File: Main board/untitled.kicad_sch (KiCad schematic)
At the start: 54 parts, among them J1 Conn_02x20_Odd_Even, J10 RA, J11 EL, J12 AZ, J13 GPS, J14 SHUTTER, J15 PWR_ON, J16 BOOT, J2 RJE05-166-1310, J9 DEC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

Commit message: updt
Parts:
- added C53: 100n, Capacitor_SMD:C_0402_1005Metric, symbol Device:C
- added R59, R60: 100k, Resistor_SMD:R_0402_1005Metric, symbol Device:R
- R43, R44: value 2k -> 2k2
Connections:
- net +3V3: now also R34.1, R35.1, R36.1, R37.1
- net DC_LED: now also U1.56 (PB4); no longer U1.57 (PB5)
- net GND: now also C53.2, R60.2; no longer R34.1, R35.1, R36.1, R37.1
- net USB_LED: now also U1.57 (PB5); no longer U1.56 (PB4)
- net VIN_ADC: now reaches U1.11 (PC3)
- net VIN_ADC: now also C53.1, R59.2, R60.1
- new net +12V: R59.1
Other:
- moved on the sheet: J10, J11, J12, J9, R34, R35, R36, R37

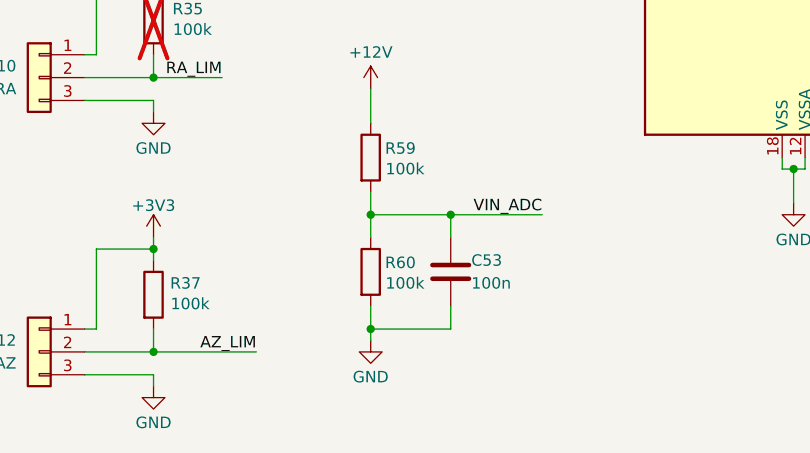
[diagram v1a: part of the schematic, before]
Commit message: Updated resistor values
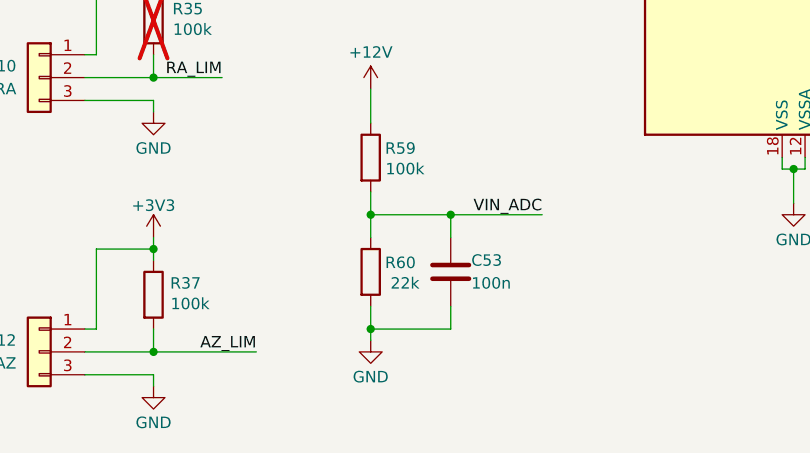
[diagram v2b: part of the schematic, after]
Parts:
- R60: value 100k -> 22k
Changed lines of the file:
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@@
 			)
 		)
-		(property "Value" "100k"
+		(property "Value" "22k"
 			(at 106.68 167.64 0)
 			(effects

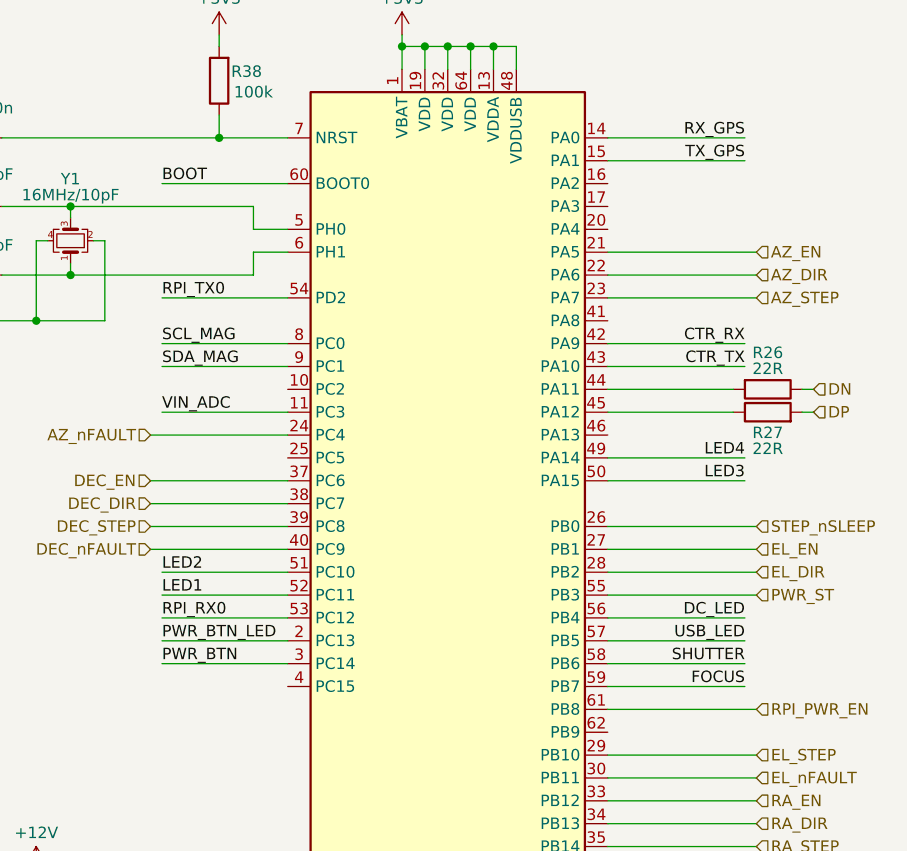
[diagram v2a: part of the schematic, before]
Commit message: Updated endstops routing
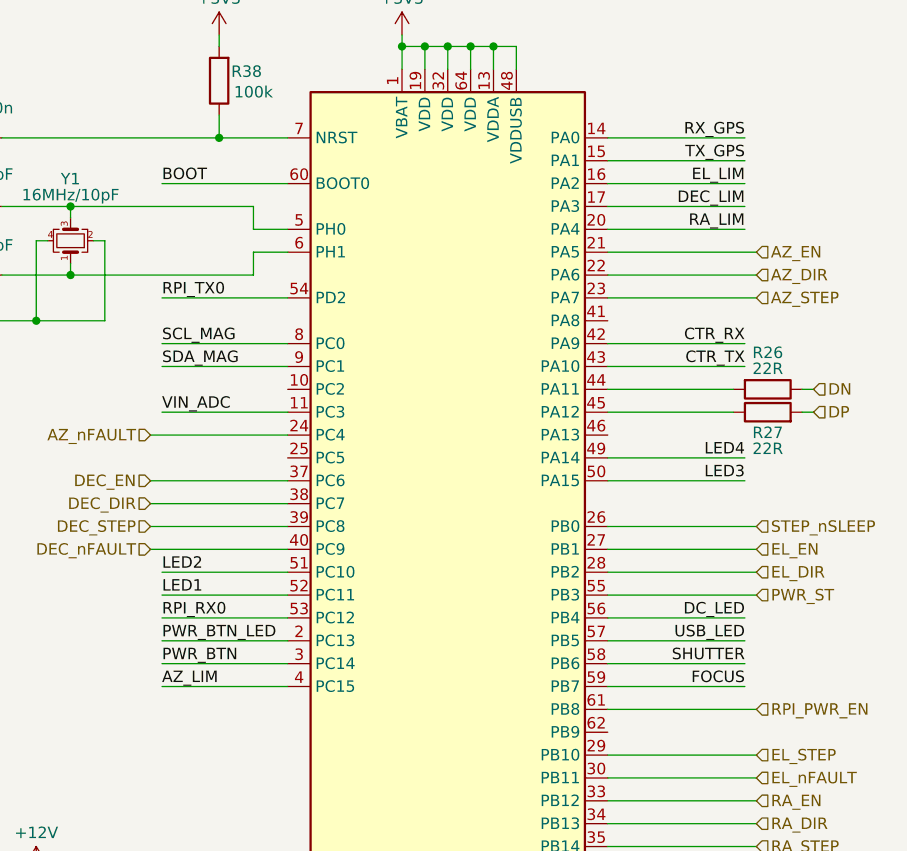
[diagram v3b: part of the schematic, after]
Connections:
- net AZ_LIM: now also U1.4 (PC15)
- net DEC_LIM: now also U1.17 (PA3)
- net EL_LIM: now also U1.16 (PA2)
- net RA_LIM: now also U1.20 (PA4)
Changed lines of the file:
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@@
+	(wire
+		(pts
+			(xy 166.37 74.93) (xy 181.61 74.93)
+		)
+		(stroke
+			(width 0)
+			(type default)
+		)
+	)
 	(wire
 		(pts
@@
 	(wire
 		(pts
+			(xy 166.37 69.85) (xy 181.61 69.85)
+		)
+		(stroke
+			(width 0)
+			(type default)
+		)
+	)
+	(wire
+		(pts
 			(xy 254 135.89) (xy 254 137.16)
 		)
@@
 	(wire
 		(pts
+			(xy 166.37 72.39) (xy 181.61 72.39)
+		)
+		(stroke
+			(width 0)
+			(type default)
+		)
+	)
+	(wire
+		(pts
 			(xy 43.18 163.83) (xy 43.18 165.1)
 		)
@@
 		(pts
 			(xy 127 72.39) (xy 127 74.93)
+		)
+		(stroke
+			(width 0)
+			(type default)
+		)
+	)
+	(wire
+		(pts
+			(xy 116.84 125.73) (xy 130.81 125.73)
 		)
 		(stroke
@@
 		)
 	)
+	(label "DEC_LIM"
+		(at 181.61 72.39 180)
+		(effects
+			(font
+				(size 1.27 1.27)
+			)
+			(justify right bottom)
+		)
+	)
 	(label "CAM_GND"
 		(at 33.02 106.68 0)
@@
 		)
 	)
+	(label "EL_LIM"
+		(at 181.61 69.85 180)
+		(effects
+			(font
+				(size 1.27 1.27)
+			)
+			(justify right bottom)
+		)
+	)
 	(label "PWR_BTN"
 		(at 116.84 123.19 0)
@@
 		)
 	)
+	(label "RA_LIM"
+		(at 181.61 74.93 180)
+		(effects
+			(font
+				(size 1.27 1.27)
+			)
+			(justify right bottom)
+		)
+	)
 	(label "LED3"
 		(at 200.66 101.6 0)
@@
 		(effects
 			(font
+				(size 1.27 1.27)
+			)
+			(justify left bottom)
+		)
+	)
+	(label "AZ_LIM"
+		(at 116.84 125.73 0)
+		(effects
+			(font

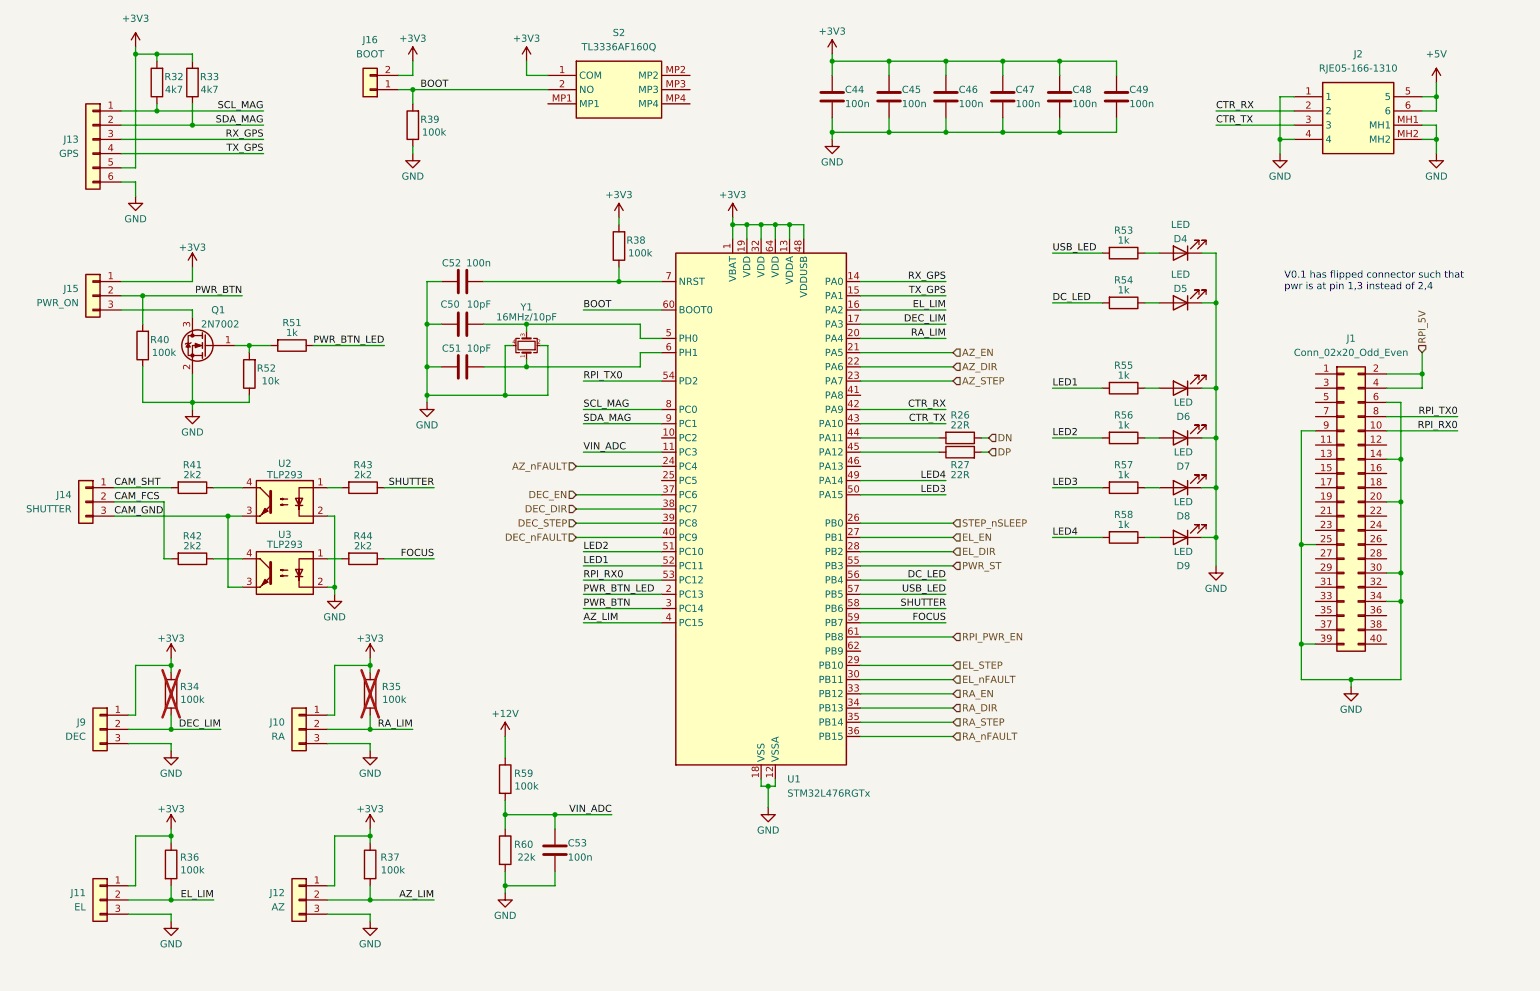
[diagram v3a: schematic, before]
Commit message: Main board updated to v0.3
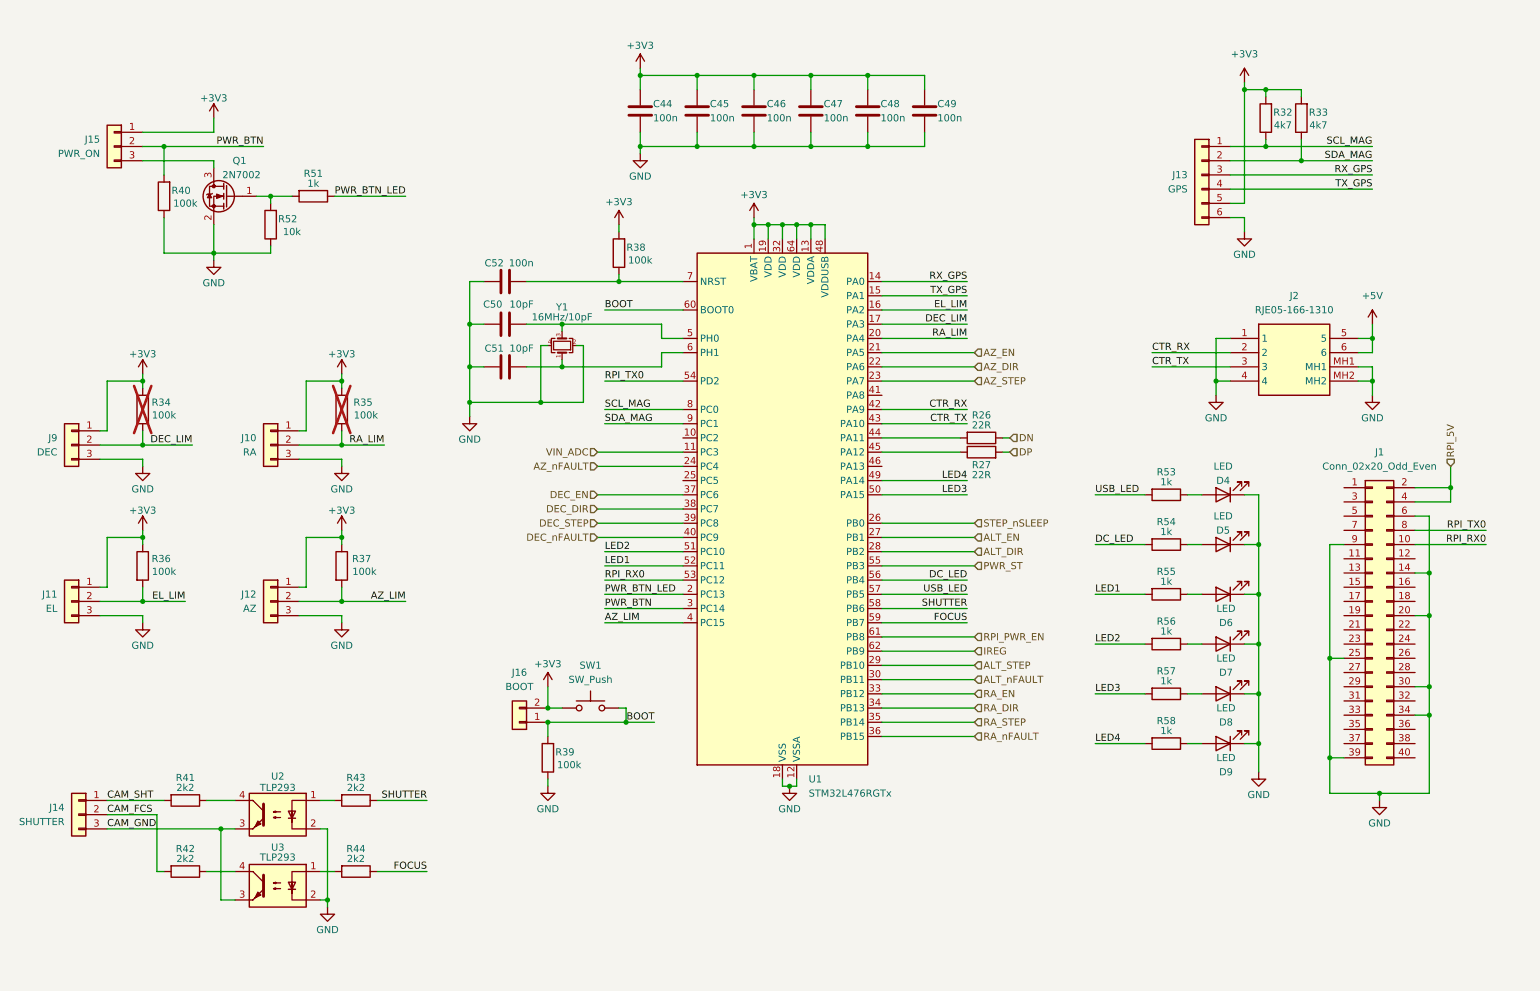
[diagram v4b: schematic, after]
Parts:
- removed C53: 100n, Capacitor_SMD:C_0402_1005Metric, symbol Device:C
- removed R59: 100k, Resistor_SMD:R_0402_1005Metric, symbol Device:R
- removed R60: 22k, Resistor_SMD:R_0402_1005Metric, symbol Device:R
- removed S2: TL3336AF160Q, TL3336AF160Q, symbol SamacSys_Parts:TL3336AF160Q
- added SW1: SW_Push, TL3336AF160Q, symbol Switch:SW_Push
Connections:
- net +3V3: now also SW1.1
- net BOOT: now also SW1.2
- net IREG: now reaches U1.62 (PB9)
- net EL_DIR renamed ALT_DIR
- net EL_EN renamed ALT_EN
- net EL_STEP renamed ALT_STEP
- net EL_nFAULT renamed ALT_nFAULT
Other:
- note removed: "V0.1 has flipped connector such that pwr is at pin 1,3 instead of 2,4"
- moved on the sheet: C44, C45, C46, C47, C48, C49, C50, C51, C52, D4, D5, D6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

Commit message: Main board updated to v0.3
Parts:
- SW1: footprint TL3336AF160Q -> SKRTLAE010
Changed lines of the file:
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@@
 		(on_board yes)
 		(dnp no)
-		(fields_autoplaced yes)
 		(property "Reference" "SW1"
 			(at 118.11 133.35 0)
@@
 			)
 		)
-		(property "Footprint" "TL3336AF160Q"
+		(property "Footprint" "SKRTLAE010"
 			(at 118.11 135.89 0)
 			(effects

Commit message: Main board v0.3 to be manufactured
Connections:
- net CAM_SHT renamed CAM_SHTR
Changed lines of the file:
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@@
 		)
 	)
-	(label "CAM_SHT"
+	(label "CAM_SHTR"
 		(at 31.75 157.48 0)
 		(effects

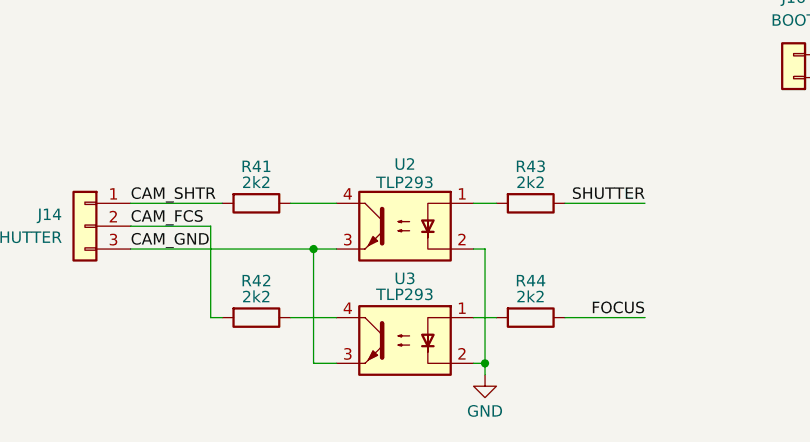
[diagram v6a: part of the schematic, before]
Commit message: Added part numbers for simpler ordering
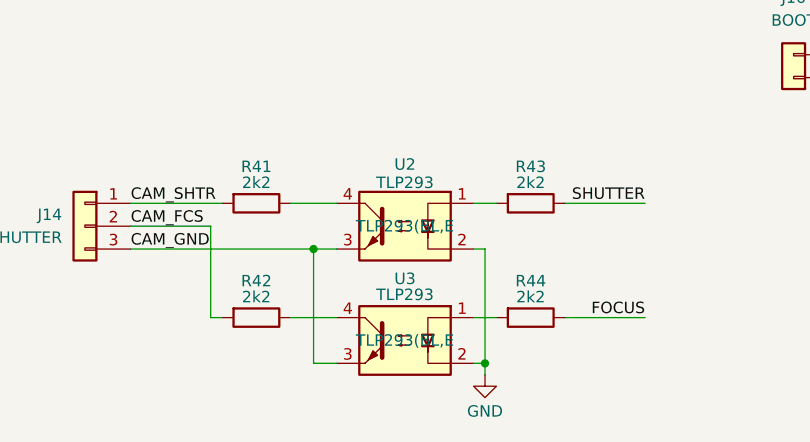
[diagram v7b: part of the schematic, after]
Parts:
- C44, C45, C46, C47, C48, C49, C52: Part Number (none) -> GRM155R71C104JA88D
- C50, C51: Part Number (none) -> GCM1555C1H100FA16D
- D4, D5, D6, D7, D8, D9: Part Number (none) -> SML-D12U1WT86
- J1, J10, J11, J12, J13, J14, J15, J16, J2, J9, SW1: now left out of the parts list
- Q1: Part Number (none) -> 2N7002AKW-QX
- R26, R27: Part Number (none) -> CRCW040222R0FKED
- R32, R33: Part Number (none) -> CRCW04024K70FKED
- R34, R35, R36, R37, R38, R39, R40: Part Number (none) -> CRCW0402100KFKEE
- R41, R42, R43, R44: Part Number (none) -> CRCW04022K20FKEDC
- R51, R53, R54, R55, R56, R57, R58: Part Number (none) -> CRCW04021K00FKED
- R52: Part Number (none) -> CRCW040210K0FKEDC
- U1: Part Number (none) -> STM32L476RGT6
- U2, U3: Part Number (none) -> TLP293(BL,E
- Y1: Part Number (none) -> ECS1601037B2CTNTR

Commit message: Updated Main board to v1.0
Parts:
- removed J1: Conn_02x20_Odd_Even, Connector_PinSocket_2.54mm:PinSocket_2x20_P2.54mm_Vertical, symbol Connector_Generic:Conn_02x20_Odd_Even
- removed J16: BOOT, Connector_PinHeader_2.54mm:PinHeader_1x02_P2.54mm_Vertical, symbol Connector_Generic:Conn_01x02
- added J1: RPi, Connector_JST:JST_PH_B4B-PH-K_1x04_P2.00mm_Vertical, symbol Connector_Generic:Conn_01x04
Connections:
- net FOCUS: now also U1.58 (PB6); no longer U1.59 (PB7)
- net GND: now also J1.4 (Pin_4)
- net RPI_5V: now also J1.1 (Pin_1)
- net RPI_RX0: now also J1.3 (Pin_3)
- net RPI_TX0: now also J1.2 (Pin_2)
- net SHUTTER: now also U1.59 (PB7); no longer U1.58 (PB6)
